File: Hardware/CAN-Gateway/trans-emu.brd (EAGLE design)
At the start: 29 x 34 mm, 33 parts, among them IC1 MIC5233-3.3YM5-TR, U1 STM32F413RGT6, U2 TJA1042HVSON, U3 TJA1042HVSON, U4 TJA1042HVSON, Y1 CRYSTAL-3.2X2.54-PIN

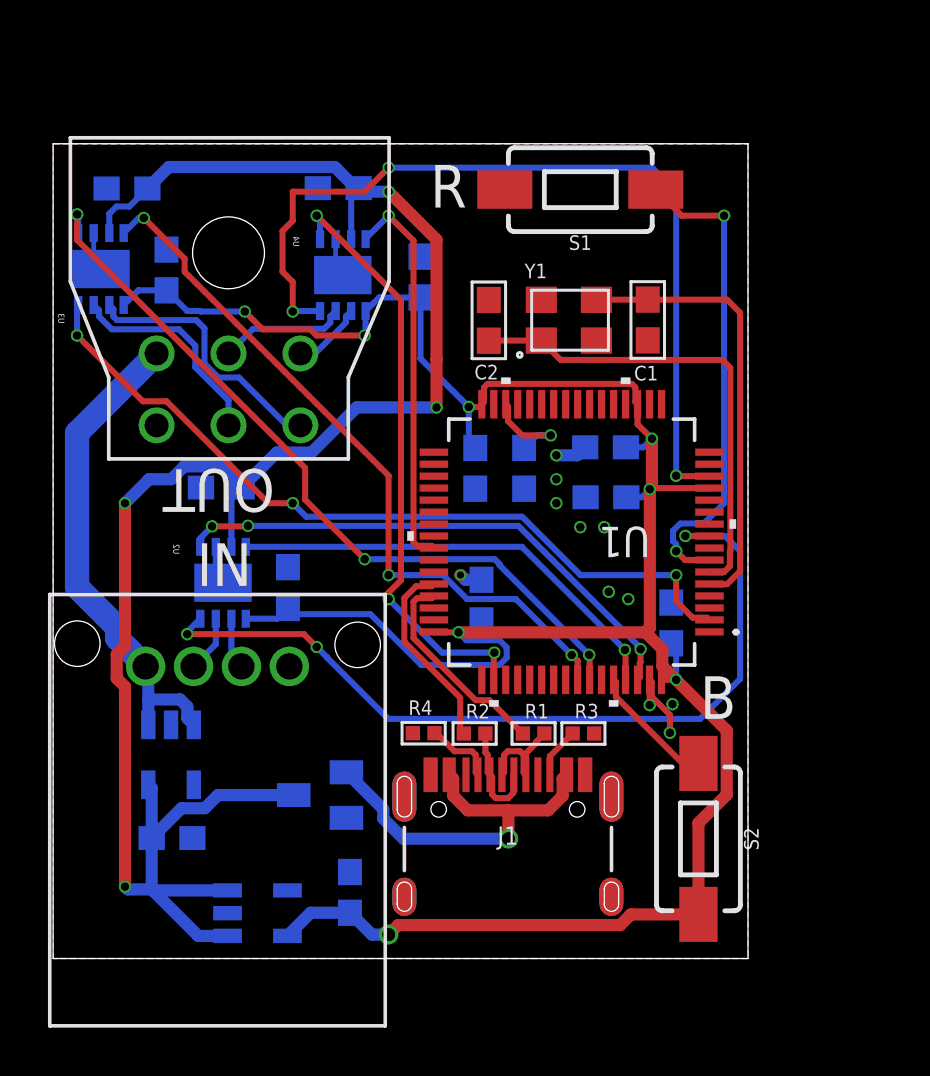
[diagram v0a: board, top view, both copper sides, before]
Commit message: Ibooster board updates
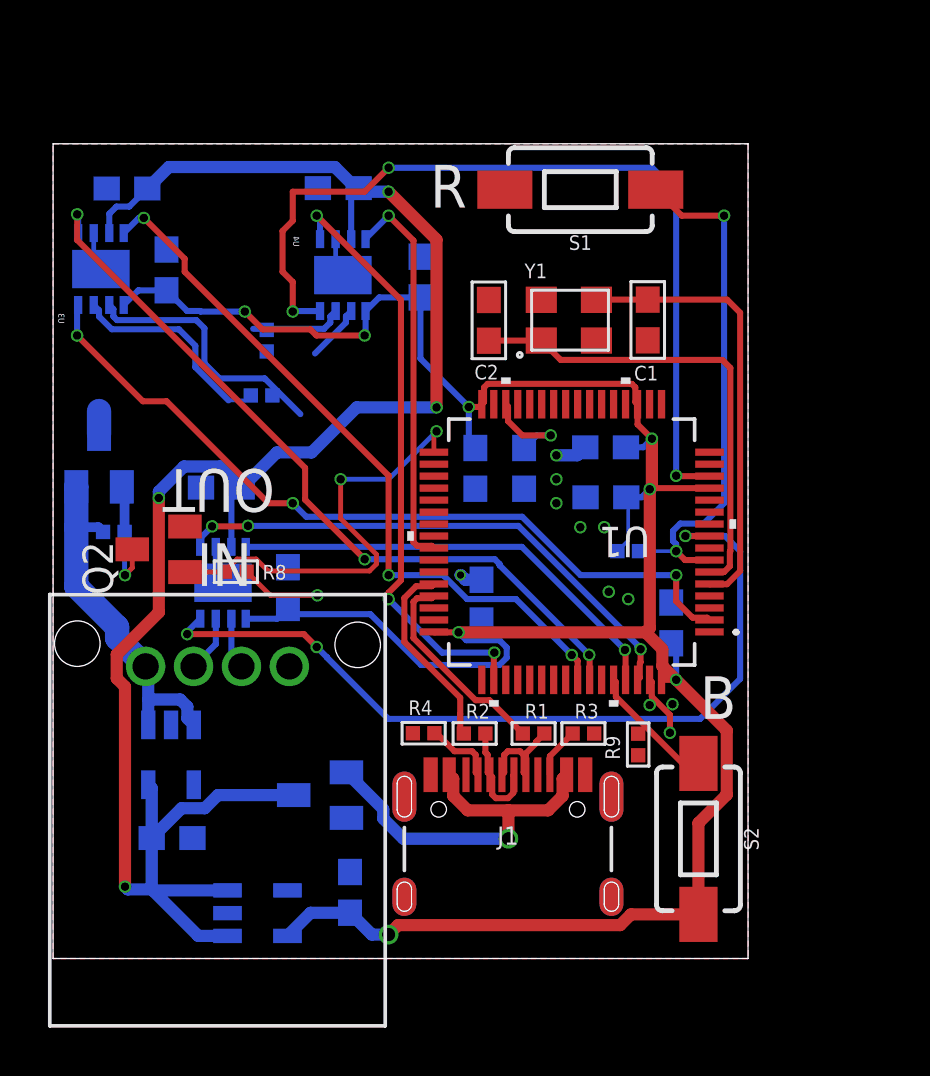
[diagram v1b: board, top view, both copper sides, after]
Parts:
- removed U$2: MICROFIT-6, interceptor:MICROFIT-6
- added Q1: PMOSFET, Transistor:SOT23
- added Q2: NMOSFET, Transistor:SOT23
- added R10, R7, R8, R9: 10k, comma.ai:0402-R
- added R5, R6: 120, comma.ai:0402-R
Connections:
- new net N$15: Q1.3
- new net N$16: Q1.1, Q2.3, R7.1
- new net PWRON: Q2.1, R8.2, U1.33
- net 12V: now also Q1.2, R7.2; no longer U$2.4
- net 3.3V: now also R10.2
- net CAN2_H: now also R5.1; no longer U$2.2
- net CAN2_L: now also R5.2; no longer U$2.3
- net CAN3_H: now also R6.1; no longer U$2.5
- net CAN3_L: now also R6.2; no longer U$2.6
- net GND: now also Q2.2, R8.1, R9.1; no longer U$2.1
- net N$8: now also R10.1
- net N$9: now also R9.2
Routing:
- net PWRON: track 0.00 -> 18.6 mm, vias 0 -> 2
- net 12V: track 20.7 -> 15.0 mm
- net N$16: track 0.00 -> 4.94 mm, vias 0 -> 1
- net GND: track 10.7 -> 13.3 mm, vias 11 -> 12
- net 3.3V: track 104.2 -> 106.6 mm
- net N$8: track 20.4 -> 21.9 mm
- net CAN3_H: track 5.36 -> 3.94 mm
- net N$15: track 0.00 -> 0.97 mm
- net CAN3_L: track 3.01 -> 2.40 mm
- net 5V: track 79.5 -> 78.9 mm

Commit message: Gateway rev2
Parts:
- removed U$1: MINI50-4, interceptor:MINI50
- added J2, J3, J4: (no value), SparkFun-Connectors:1X02
- added J5: (no value), SparkFun-Connectors:1X04
- added SJ1, SJ2: (no value), jumper:SJ
- U2, U3, U4: value TJA1042HVSON -> TJA1042; device comma.ai:HVSON8 -> CM,118:NXP_SEMICONDUCTORS_TJA1042T-3-CM_118_0
- moved S1 28.8 mm to (31.7, 5.02), turned to 270 degrees
- moved C16 17.2 mm to (24.8, 14.7), flipped to the top, turned to 270 degrees
- moved IC1 16.0 mm to (18.2, 14.7), flipped to the top, turned to 0 degrees
- moved C3 14.6 mm to (18.5, 35.0), flipped to the top, turned to 180 degrees
- moved C7 14.5 mm to (27.8, 35.0), flipped to the top
- moved C8 14.5 mm to (27.8, 32.9), flipped to the top
- moved C2 13.9 mm to (31.9, 28.5), turned to 0 degrees
- moved C11 12.9 mm to (14.3, 25.9), flipped to the top, turned to 90 degrees
- moved Q1 12.7 mm to (5.26, 8.57), flipped to the top
- moved Y1 12.6 mm to (32.9, 26.3), turned to 270 degrees
- moved C10 12.6 mm to (9.09, 28.0), flipped to the top, turned to 0 degrees
- moved C6 12.4 mm to (18.5, 32.9), flipped to the top, turned to 180 degrees
- moved R7 12.4 mm to (4.92, 5.61), flipped to the top
- moved R8 10.5 mm to (8.19, 5.69)
- moved C13 9.75 mm to (9.11, 35.9), flipped to the top, turned to 0 degrees
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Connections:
- removed net N$15: Q1.3
- new net 12VOUT: J3.1, Q1.3
- new net CAN1_H: J4.1, U2.7
- new net CAN1_L: J4.2, U2.6
- net 12V: now also J2.1; no longer U$1.4
- net CAN2_H: now also J5.1
- net CAN2_L: now also J5.2, SJ1.1; no longer R5.2
- net CAN3_H: now also J5.3, SJ2.1; no longer R6.1
- net CAN3_L: now also J5.4
- net GND: now also J2.2, J3.2; no longer U$1.1, U2.PAD, U3.PAD, U4.PAD
- net N$12: now also R5.2, SJ1.2; no longer U$1.3, U2.7
- net N$14: now also R6.1, SJ2.2; no longer U$1.2, U2.6
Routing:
- net 5V: track 78.9 -> 53.0 mm, vias 4 -> 0
- net CAN2_TX: track 32.3 -> 14.0 mm, vias 3 -> 2
- net CAN2_RX: track 30.4 -> 16.4 mm, vias 3 -> 2
- net PWRON: track 18.6 -> 32.5 mm
- net N$2: track 19.8 -> 5.96 mm
- net GND: track 13.3 -> 0.00 mm, vias 12 -> 7
- net CAN3_EN: track 36.6 -> 23.8 mm, vias 3 -> 2
- net N$1: track 18.5 -> 5.90 mm
- net CAN1_EN: track 35.0 -> 47.1 mm, vias 3 -> 0
- net N$8: track 21.9 -> 33.1 mm, vias 2 -> 0
- net CAN3_TX: track 25.2 -> 15.6 mm, vias 3 -> 2
- net 3.3V: track 106.6 -> 113.6 mm, vias 8 -> 2
- net N$4: track 8.68 -> 15.5 mm
- net N$3: track 8.16 -> 14.7 mm, vias 0 -> 2
- net N$9: track 5.78 -> 12.3 mm, vias 0 -> 2
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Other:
- board size 29 x 34 mm -> 34 x 38 mm
- board text added: "12V"
- board text added: "12VOUT"
- board text added: "CAN1H"
- board text added: "CAN1L"
- board text added: "CAN2H"
- board text added: "CAN2L"
- board text added: "CAN3H"
- board text added: "CAN3L"
- board text added: "GND"
- board text added: "Ocelot CAN Gateway"
- board text removed: "IN"
- board text removed: "OUT"
- board text removed: "Ocelot CAN Translator"

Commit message: swd header
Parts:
- added J6: (no value), SparkFun-Connectors:1X05_1.27MM
- moved C16 0.72 mm to (25.0, 14.0)
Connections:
- removed net N$8: R10.1, S1.1, U1.7
- new net NRST: J6.4, R10.1, S1.1, U1.7
- new net SCK: J6.2, U1.49
- new net SWD: J6.3, U1.46
- net 3.3V: now also J6.5
- net GND: now also J6.1
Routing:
- net NRST: track 0.00 -> 34.5 mm
- net N$8: track 33.1 -> 0.00 mm
- net SWD: track 0.00 -> 19.4 mm, vias 0 -> 1
- net SCK: track 0.00 -> 16.1 mm, vias 0 -> 1
- net 3.3V: track 113.6 -> 117.2 mm
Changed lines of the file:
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@@
 <attribute name="NAME" x="10.219440625" y="3.903421875" size="0.6096" layer="25"/>
 </element>
-<element name="C16" library="comma.ai" package="0603-C" value="2.2u" x="24.801796875" y="14.71088125" smashed="yes" rot="R270">
-<attribute name="NAME" x="23.986396875" y="12.37951875" size="0.6096" layer="25"/>
+<element name="C16" library="comma.ai" package="0603-C" value="2.2u" x="25.045634375" y="14.035240625" smashed="yes" rot="R270">
+<attribute name="NAME" x="24.230234375" y="11.703878125" size="0.6096" layer="25"/>
 </element>
 <element name="C2" library="comma.ai" package="0603-C" value="22p" x="31.90911875" y="28.509484375" smashed="yes">
@@
 <attribute name="PROD_ID" value="CONN-09696" x="1.668578125" y="24.9423" size="1.778" layer="27" rot="R90" display="off"/>
 <attribute name="VALUE" x="3.700578125" y="23.6723" size="0.6096" layer="27" font="vector" ratio="20" rot="R90"/>
+</element>
+<element name="J6" library="SparkFun-Connectors" library_urn="urn:adsk.eagle:library:513" package="1X05_1.27MM" package3d_urn="urn:adsk.eagle:package:38110/1" value="" x="32.57458125" y="13.724140625" smashed="yes" rot="R90">
+<attribute name="NAME" x="31.17758125" y="12.454140625" size="0.6096" layer="25" font="vector" ratio="20" rot="R90"/>
+<attribute name="VALUE" x="34.60658125" y="12.454140625" size="0.6096" layer="27" font="vector" ratio="20" rot="R90"/>
 </element>
 </elements>
@@
 <via x="18.759059375" y="31.3147" extent="1-16" drill="0.35"/>
 <via x="24.759059375" y="34.3147" extent="1-16" drill="0.35"/>
+<contactref element="J6" pad="1"/>
 </signal>
 <signal name="CAN1_RX">
@@
 <wire x1="15.982415625" y1="8.934559375" x2="13.734640625" y2="8.934559375" width="0.4064" layer="1"/>
 </signal>
-<signal name="N$8">
+<signal name="NRST">
 <contactref element="U1" pad="7"/>
 <contactref element="S1" pad="1"/>
@@
 <wire x1="33.400103125" y1="24.872484375" x2="33.7206" y2="24.5519875" width="0.1524" layer="1"/>
 <wire x1="33.7206" y1="10.191340625" x2="31.69911875" y2="8.169859375" width="0.1524" layer="1"/>
-<wire x1="33.7206" y1="24.5519875" x2="33.7206" y2="10.191340625" width="0.1524" layer="1"/>
+<wire x1="33.7206" y1="24.5519875" x2="33.7206" y2="18" width="0.1524" layer="1"/>
+<wire x1="33.7206" y1="18" x2="33.7206" y2="10.191340625" width="0.1524" layer="1"/>
 <wire x1="30.0156" y1="25.187059375" x2="30.3276" y2="25.499059375" width="0.1524" layer="1"/>
 <wire x1="30.30591875" y1="29.09365" x2="30.42495" y2="29.21268125" width="0.1524" layer="1"/>
@@
 <wire x1="30.30591875" y1="25.5919375" x2="30.30591875" y2="29.09365" width="0.1524" layer="1"/>
 <wire x1="30.0156" y1="24.622159375" x2="30.0156" y2="25.187059375" width="0.1524" layer="1"/>
+<contactref element="J6" pad="4"/>
+<wire x1="32.57458125" y1="17.534140625" x2="33.254740625" y2="17.534140625" width="0.1524" layer="1"/>
+<wire x1="33.254740625" y1="17.534140625" x2="33.7206" y2="18" width="0.1524" layer="1"/>
 </signal>
 <signal name="N$9">
@@
 <wire x1="26.93038125" y1="8.142340625" x2="24.9283" y2="10.144421875" width="0.1524" layer="1"/>
 <wire x1="24.9283" y1="10.144421875" x2="24.80691875" y2="10.144421875" width="0.1524" layer="1"/>
-<wire x1="25.146" y1="16.764" x2="25.146" y2="19.304" width="0.127" layer="1"/>
-<wire x1="25.146" y1="11.049" x2="25.146" y2="16.764" width="0.127" layer="16"/>
+<wire x1="25.146" y1="16.1163" x2="25.146" y2="19.304" width="0.127" layer="1"/>
+<wire x1="25.146" y1="11.049" x2="25.146" y2="16.1163" width="0.127" layer="16"/>
 <wire x1="25.019" y1="10.922" x2="25.146" y2="11.049" width="0.127" layer="16"/>
 <wire x1="24.892" y1="10.795" x2="25.019" y2="10.922" width="0.127" layer="1"/>
@@
 <wire x1="25.146" y1="19.304" x2="25.14691875" y2="19.307921875" width="0.127" layer="1"/>
 <wire x1="24.892" y1="10.16" x2="24.80691875" y2="10.144421875" width="0.127" layer="1"/>
-<via x="25.146" y="16.764" extent="1-16" drill="0.3048"/>
+<via x="25.146" y="16.1163" extent="1-16" drill="0.3048"/>
 <via x="25.019" y="10.922" extent="1-16" drill="0.3048"/>
 </signal>
@@
 <wire x1="29.857978125" y1="9.46761875" x2="29.857978125" y2="4.7699375" width="0.1524" layer="1"/>
 <wire x1="29.857978125" y1="4.7699375" x2="26.93038125" y2="1.842340625" width="0.1524" layer="1"/>
-<wire x1="24.801796875" y1="15.198246875" x2="24.801796875" y2="15.56088125" width="0.1524" layer="1"/>
-<wire x1="24.098596875" y1="14.495046875" x2="24.801796875" y2="15.198246875" width="0.1524" layer="1"/>
+<wire x1="24.488796875" y1="14.885246875" x2="25.045634375" y2="14.885240625" width="0.1524" layer="1"/>
+<wire x1="24.098596875" y1="14.495046875" x2="24.488796875" y2="14.885246875" width="0.1524" layer="1"/>
 <wire x1="26.93038125" y1="1.842340625" x2="24.098596875" y2="4.674125" width="0.1524" layer="1"/>
 <wire x1="24.098596875" y1="4.674125" x2="24.098596875" y2="14.495046875" width="0.1524" layer="1"/>
-<wire x1="19.405996875" y1="15.6604375" x2="24.702240625" y2="15.6604375" width="0.1524" layer="1"/>
-<wire x1="24.702240625" y1="15.6604375" x2="24.801796875" y2="15.56088125" width="0.1524" layer="1"/>
+<wire x1="19.405996875" y1="15.6604375" x2="20.405996875" y2="14.6604375" width="0.1524" layer="1"/>
+<wire x1="25.045634375" y1="14.885240625" x2="24.82083125" y2="14.6604375" width="0.1524" layer="1"/>
+<wire x1="24.82083125" y1="14.6604375" x2="20.405996875" y2="14.6604375" width="0.1524" layer="1"/>
 <wire x1="4.1316" y1="18.436196875" x2="5.863921875" y2="20.16851875" width="0.1524" layer="1"/>
 <wire x1="5.863921875" y1="20.16851875" x2="5.863921875" y2="20.3443625" width="0.1524" layer="1"/>
@@
 <wire x1="19.304" y1="15.748" x2="19.405996875" y2="15.6604375" width="0.127" layer="1"/>
 <wire x1="27.94" y1="18.161" x2="27.94" y2="19.431" width="0.127" layer="1"/>
-<wire x1="25.654" y1="15.875" x2="27.94" y2="18.161" width="0.127" layer="1"/>
-<wire x1="25.146" y1="15.875" x2="25.654" y2="15.875" width="0.127" layer="1"/>
-<wire x1="24.892" y1="15.621" x2="25.146" y2="15.875" width="0.127" layer="1"/>
-<wire x1="24.892" y1="15.621" x2="24.801796875" y2="15.56088125" width="0.127" layer="1"/>
+<wire x1="25.807746875" y1="16.028746875" x2="27.94" y2="18.161" width="0.127" layer="1"/>
+<wire x1="25.807746875" y1="16.028746875" x2="25.045634375" y2="14.885240625" width="0.127" layer="1"/>
 <wire x1="8.255" y1="33.274" x2="8.255" y2="28.067" width="0.127" layer="1"/>
 <wire x1="7.493" y1="34.036" x2="8.255" y2="33.274" width="0.127" layer="1"/>
@@
 <via x="28.829" y="19.431" extent="1-16" drill="0.3048"/>
 <via x="28.194" y="27.305" extent="1-16" drill="0.3048"/>
+<contactref element="J6" pad="5"/>
+<wire x1="32.57458125" y1="18.804140625" x2="31.96640625" y2="19.412315625" width="0.1524" layer="1"/>
+<wire x1="31.96640625" y1="19.412315625" x2="29.801825" y2="19.412315625" width="0.1524" layer="1"/>
 </signal>
 <signal name="12V">
@@
 <wire x1="5" y1="32.941315625" x2="4.1879625" y2="32.129278125" width="0.1524" layer="16"/>
 </signal>
+<signal name="SWD">
+<contactref element="U1" pad="46"/>
+<contactref element="J6" pad="3"/>
+<via x="31.71951875" y="20.469859375" extent="1-16" drill="0.35"/>
+<wire x1="17.64691875" y1="22.307921875" x2="27.110253125" y2="22.307921875" width="0.1524" layer="1"/>
+<wire x1="27.110253125" y1="22.307921875" x2="28.46585" y2="20.952325" width="0.1524" layer="1"/>
+<wire x1="31.237053125" y1="20.952325" x2="31.71951875" y2="20.469859375" width="0.1524" layer="1"/>
+<wire x1="28.46585" y1="20.952325" x2="31.237053125" y2="20.952325" width="0.1524" layer="1"/>
+<wire x1="31.71951875" y1="20.469859375" x2="31.71951875" y2="17.119203125" width="0.1524" layer="16"/>
+<wire x1="31.71951875" y1="17.119203125" x2="32.57458125" y2="16.264140625" width="0.1524" layer="16"/>
+</signal>
+<signal name="SCK">
+<contactref element="U1" pad="49"/>
+<contactref element="J6" pad="2"/>
+<via x="23.41118125" y="15.20698125" extent="1-16" drill="0.35"/>
+<wire x1="19.64691875" y1="19.307921875" x2="19.791321875" y2="19.16351875" width="0.1524" layer="1"/>
+<wire x1="19.791321875" y1="19.16351875" x2="19.791321875" y2="18.626853125" width="0.1524" layer="1"/>
+<wire x1="19.791321875" y1="18.626853125" x2="19.910353125" y2="18.507821875" width="0.1524" layer="1"/>
+<wire x1="19.910353125" y1="18.507821875" x2="20.110340625" y2="18.507821875" width="0.1524" layer="1"/>
+<wire x1="20.110340625" y1="18.507821875" x2="23.41118125" y2="15.20698125" width="0.1524" layer="1"/>
+<wire x1="23.41118125" y1="15.20698125" x2="23.62601875" y2="15.20698125" width="0.1524" layer="16"/>
+<wire x1="23.62601875" y1="15.20698125" x2="24.9671375" y2="16.5481" width="0.1524" layer="16"/>
+<wire x1="24.9671375" y1="16.5481" x2="31.020621875" y2="16.5481" width="0.1524" layer="16"/>
+<wire x1="31.020621875" y1="16.5481" x2="32.57458125" y2="14.994140625" width="0.1524" layer="16"/>
+</signal>
 </signals>
